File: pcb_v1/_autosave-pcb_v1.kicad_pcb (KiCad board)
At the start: 2 copper layers, 57.5 x 32 mm, 14 parts, among them IC1 ESP32-C3-WROOM-02-N4, IC2 DWM3000TR13, IC3 TC1017-3.3VLTTR, J1 Conn_01x04_Pin, J2 1769, J3 Conn_01x04_Pin

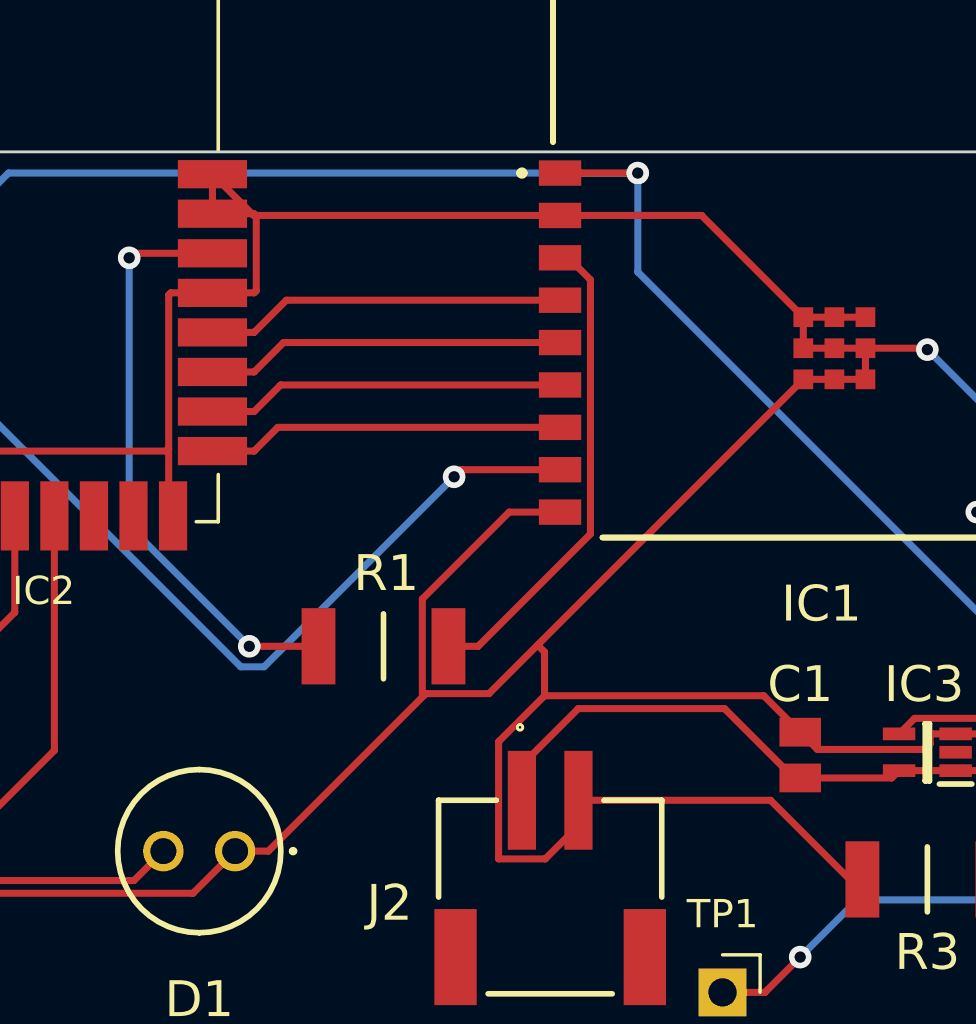
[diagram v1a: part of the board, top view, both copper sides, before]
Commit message: fix wiring issue, EN pin on esp32 always grounded
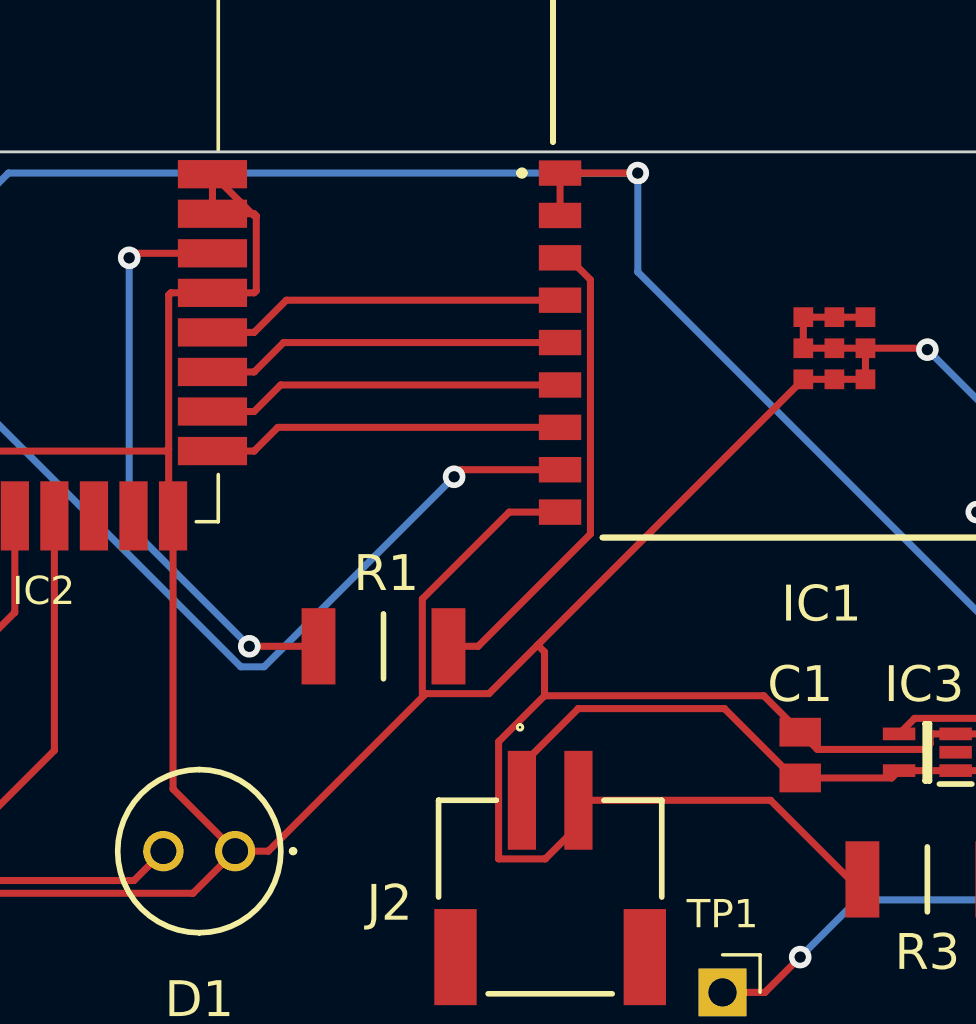
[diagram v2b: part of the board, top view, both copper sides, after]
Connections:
- IC1 pad 2: GND -> VDD
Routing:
- net GND: track 199.6 -> 191.4 mm
- net VDD: track 102.5 -> 104.0 mm
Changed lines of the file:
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@@
       (psa4output false)
       (plotreference true)
-      (plotvalue true)
+      (plotvalue false)
       (plotinvisibletext false)
       (sketchpadsonfab false)
@@
       (net 3 "VDD") (pinfunction "3V3") (pintype "passive"))
     (pad "2" smd rect (at -9.71 -4.7 90) (size 0.9 1.5) (layers "F.Cu" "F.Paste" "F.Mask")
-      (net 2 "GND") (pinfunction "EN") (pintype "passive"))
+      (net 3 "VDD") (pinfunction "EN") (pintype "passive"))
     (pad "3" smd rect (at -9.71 -3.2 90) (size 0.9 1.5) (layers "F.Cu" "F.Paste" "F.Mask")
       (net 4 "Net-(IC1-IO4)") (pinfunction "IO4") (pintype "passive"))
@@
   (segment (start 110.8025 97.885) (end 110.6475 97.73) (width 0.25) (layer "F.Cu") (net 2))
   (segment (start 137.6 105.675) (end 137.6 105.95) (width 0.25) (layer "F.Cu") (net 2))
-  (segment (start 129.51 87.25) (end 133.11 90.85) (width 0.25) (layer "F.Cu") (net 2))
   (segment (start 119.75 104.175) (end 121.985 104.175) (width 0.25) (layer "F.Cu") (net 2))
   (segment (start 112.1975 85.79) (end 113.6575 87.25) (width 0.25) (layer "F.Cu") (net 2))
@@
   (segment (start 119.625 100.825) (end 119.625 104.175) (width 0.25) (layer "F.Cu") (net 2))
   (segment (start 122.325 105.875) (end 122.325 110.025) (width 0.25) (layer "F.Cu") (net 2))
+  (segment (start 113 109.75) (end 110.8025 107.5525) (width 0.25) (layer "F.Cu") (net 2))
   (segment (start 148.505 112.755) (end 145.5 109.75) (width 0.25) (layer "F.Cu") (net 2))
   (segment (start 119.625 104.175) (end 119.75 104.175) (width 0.25) (layer "F.Cu") (net 2))
@@
   (segment (start 138.5 105.6) (end 137.675 105.6) (width 0.25) (layer "F.Cu") (net 2))
   (segment (start 123.95 104.25) (end 123.95 102.7) (width 0.25) (layer "F.Cu") (net 2))
-  (segment (start 124.5 87.25) (end 129.51 87.25) (width 0.25) (layer "F.Cu") (net 2))
   (segment (start 135.2 110.75) (end 134.75 110.75) (width 0.25) (layer "F.Cu") (net 2))
   (segment (start 135.31 93.05) (end 134.21 93.05) (width 0.25) (layer "F.Cu") (net 2))
@@
   (segment (start 113.6725 87.19) (end 113.7475 87.265) (width 0.25) (layer "F.Cu") (net 2))
   (segment (start 142.025 107.16) (end 140.465 105.6) (width 0.25) (layer "F.Cu") (net 2))
+  (segment (start 110.8025 107.5525) (end 110.8025 97.885) (width 0.25) (layer "F.Cu") (net 2))
   (segment (start 110.7225 89.99) (end 112.1975 89.99) (width 0.25) (layer "F.Cu") (net 2))
   (segment (start 133.11 91.95) (end 134.21 91.95) (width 0.25) (layer "F.Cu") (net 2))
@@
   (segment (start 110.5575 95.59) (end 110.6475 95.5) (width 0.25) (layer "F.Cu") (net 2))
   (segment (start 123.975 110.025) (end 125.15 108.85) (width 0.25) (layer "F.Cu") (net 2))
-  (segment (start 113.6575 87.25) (end 124.5 87.25) (width 0.25) (layer "F.Cu") (net 2))
   (segment (start 137.45 91.95) (end 137.5 92) (width 0.25) (layer "F.Cu") (net 2))
   (segment (start 133.11 90.85) (end 134.21 90.85) (width 0.25) (layer "F.Cu") (net 2))
@@
   (segment (start 145.5 100) (end 137.5 92) (width 0.25) (layer "B.Cu") (net 2))
   (segment (start 124.5 85.75) (end 127.25 85.75) (width 0.25) (layer "F.Cu") (net 3))
+  (segment (start 124.5 87.25) (end 124.5 85.75) (width 0.25) (layer "F.Cu") (net 3))
   (segment (start 142.25 104.25) (end 142 104) (width 0.25) (layer "F.Cu") (net 3))
   (segment (start 101.93 103.25) (end 102 103.32) (width 0.25) (layer "F.Cu") (net 3))
